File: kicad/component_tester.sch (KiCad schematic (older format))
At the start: 17 parts, among them J1 USB_B_Micro, U3 ATmega328P-MMH

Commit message: Start panelizing
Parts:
- removed C1: 1nF, KiCad/Capacitors_SMD.pretty:C_0201, symbol component_tester-eagle-import:C2.5_2
- removed C3: 100nF, KiCad/Capacitors_SMD.pretty:C_0201, symbol component_tester-eagle-import:C5_3
- removed J1: USB_B_Micro, digikey/digikey-kicad-library/digikey-footprints.pretty:USB_Micro_B_Female_10118192, symbol Connector_Specialized:USB_B_Micro
- removed JP3: ISP, apexelectrix/apex-pin-headers.pretty:2x3-PIN-1.27mm, symbol component_tester-eagle-import:ML6
- removed JP4: Test-Pins, KiCad/kicad-footprints/Connector_PinHeader_2.54mm.pretty:PinHeader_1x03_P2.54mm_Vertical_SMD_Pin1Left, symbol component_tester-eagle-import:PINHD-1X3-PCB
- removed JP5: Start Pushbutton, freetronics/freetronics_kicad_library/freetronics_footprints.pretty:SW_PUSHBUTTON_SMD, symbol component_tester-eagle-import:PINHD-1X2-PCB
- removed R1, R3, R5: 680, component_tester:0207_10, symbol component_tester-eagle-import:R-EU_0207_10
- removed R11: 10k, component_tester:0207_2V, symbol component_tester-eagle-import:R-EU_0207_2V
- removed R12: 3k3, component_tester:0207_2V, symbol component_tester-eagle-import:R-EU_0207_2V
- removed R13: 10k, component_tester:0207_10, symbol component_tester-eagle-import:R-EU_0207_10
- removed R17: 27k, component_tester:0207_2V, symbol component_tester-eagle-import:R-EU_0207_2V
- removed R2, R4, R6: 470k, component_tester:0207_10, symbol component_tester-eagle-import:R-EU_0207_10
- removed U3: ATmega328P-MMH, Package_DFN_QFN:QFN-28-1EP_4x4mm_P0.45mm_EP2.25x2.25mm, symbol MCU_Microchip_ATmega:ATmega328P-MMH
- added J1: Conn_01x01, drawings:middle, symbol Conn_01x01
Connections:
- net labels removed: +5V, +9V, GND, PB0, PB1, PB2, PB3, PB4, PB5, PC0, PC1, PC2, PC5, PC6, PD7
- wire segments 95 -> 0
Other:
- note removed: "1"
- note removed: "2"
- note removed: "3"

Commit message: Import eagle project from o28 fifi bauteiltester
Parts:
- removed J1: Conn_01x01, drawings:middle, symbol Conn_01x01
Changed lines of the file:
@@
-EESchema Schematic File Version 2
+EESchema Schematic File Version 4
 LIBS:power
 LIBS:device
@@
 LIBS:contrib
 LIBS:valves
-LIBS:component_tester-cache
-EELAYER 25 0
+EELAYER 26 0
 EELAYER END
 $Descr A4 11693 8268
 encoding utf-8
-Sheet 1 1
+Sheet 1 3
 Title ""
 Date ""
@@
 Comment4 ""
 $EndDescr
-$Comp
-L Conn_01x01 J1
-U 1 1 5AE372AA
-P 10100 5325
-F 0 "J1" H 10100 5425 50  0000 C CNN
-F 1 "Conn_01x01" H 10100 5225 50  0000 C CNN
-F 2 "drawings:middle" H 10100 5325 50  0001 C CNN
-F 3 "" H 10100 5325 50  0001 C CNN
-	1    10100 5325
-	1    0    0    -1
-$EndComp
+$Sheet
+S 1000 1000 500  150
+U 5B1C6B30
+F0 "component_tester_1" 50
+F1 "component_tester_1.sch" 50
+$EndSheet
+$Sheet
+S 3000 1000 500  150
+U 5B1C713A
+F0 "component_tester_2" 50
+F1 "component_tester_2.sch" 50
+$EndSheet
 $EndSCHEMATC

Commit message: Add drawings back into pcb
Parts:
- added DRAWING1: DRAWING, drawings:combined, symbol Connector_Generic:Conn_01x01
- added DRAWING2: DRAWING, drawings:pads, symbol Connector_Generic:Conn_01x01
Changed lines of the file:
@@
 LIBS:contrib
 LIBS:valves
+LIBS:component_tester-cache
 EELAYER 26 0
 EELAYER END
@@
 F1 "component_tester_2.sch" 50
 $EndSheet
+$Comp
+L Connector_Generic:Conn_01x01 DRAWING1
+U 1 1 5B1C60C2
+P 1425 1775
+F 0 "DRAWING1" H 1504 1817 50  0000 L CNN
+F 1 "DRAWING" H 1504 1726 50  0000 L CNN
+F 2 "drawings:combined" H 1425 1775 50  0001 C CNN
+F 3 "~" H 1425 1775 50  0001 C CNN
+	1    1425 1775
+	1    0    0    -1
+$EndComp
+$Comp
+L Connector_Generic:Conn_01x01 DRAWING2
+U 1 1 5B1C63ED
+P 1400 2125
+F 0 "DRAWING2" H 1480 2167 50  0000 L CNN
+F 1 "DRAWING" H 1480 2076 50  0000 L CNN
+F 2 "drawings:pads" H 1400 2125 50  0001 C CNN
+F 3 "~" H 1400 2125 50  0001 C CNN
+	1    1400 2125
+	1    0    0    -1
+$EndComp
 $EndSCHEMATC

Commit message: Connect up test pads
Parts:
- removed DRAWING2: DRAWING, drawings:pads, symbol Connector_Generic:Conn_01x01
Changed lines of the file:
@@
-	1    0    0    -1
-$EndComp
-$Comp
-L Connector_Generic:Conn_01x01 DRAWING2
-U 1 1 5B1C63ED
-P 1400 2125
-F 0 "DRAWING2" H 1480 2167 50  0000 L CNN
-F 1 "DRAWING" H 1480 2076 50  0000 L CNN
-F 2 "drawings:pads" H 1400 2125 50  0001 C CNN
-F 3 "~" H 1400 2125 50  0001 C CNN
-	1    1400 2125
 	1    0    0    -1
 $EndComp

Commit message: Sort out ground net
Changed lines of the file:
@@
 	1    0    0    -1
 $EndComp
+Entry Wire Line
+	1350 1075 1450 1175
 $EndSCHEMATC

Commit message: Remove all the ground labels and zones
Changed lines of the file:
@@
 	1    0    0    -1
 $EndComp
-Entry Wire Line
-	1350 1075 1450 1175
 $EndSCHEMATC

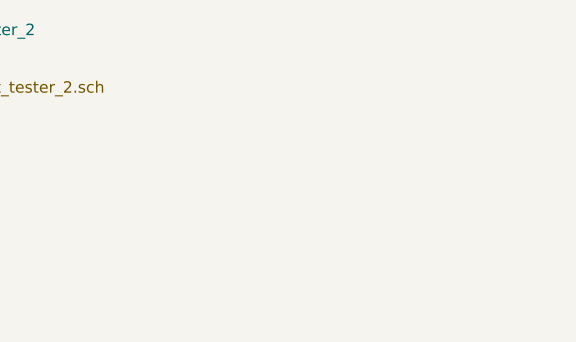
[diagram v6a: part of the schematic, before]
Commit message: Import Adafruit OLED breakout
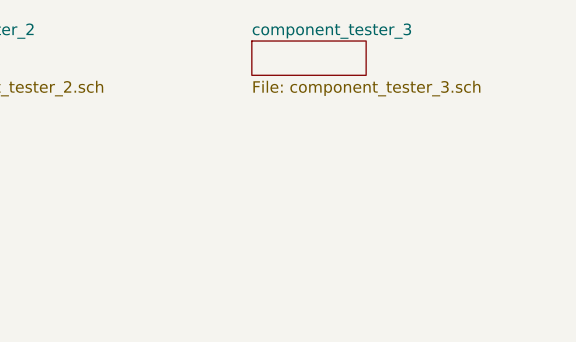
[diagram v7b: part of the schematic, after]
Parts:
- renumbered DRAWING1 to DRAWING101
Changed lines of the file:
@@
 $Descr A4 11693 8268
 encoding utf-8
-Sheet 1 3
+Sheet 1 4
 Title ""
 Date ""
@@
 $EndSheet
 $Comp
-L Connector_Generic:Conn_01x01 DRAWING1
+L Connector_Generic:Conn_01x01 DRAWING101
 U 1 1 5B1C60C2
 P 1425 1775
-F 0 "DRAWING1" H 1504 1817 50  0000 L CNN
+F 0 "DRAWING101" H 1504 1817 50  0000 L CNN
 F 1 "DRAWING" H 1504 1726 50  0000 L CNN
 F 2 "drawings:combined" H 1425 1775 50  0001 C CNN
@@
 	1    0    0    -1
 $EndComp
+$Sheet
+S 4650 1000 500  150
+U 5B23B1A6
+F0 "component_tester_3" 50
+F1 "component_tester_3.sch" 50
+$EndSheet
 $EndSCHEMATC
